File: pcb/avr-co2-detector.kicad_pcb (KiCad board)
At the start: 2 copper layers, 100 x 70 mm, 70 parts, among them J1 USB TYPE-C, J2 Backlight, J3 Backlight, J4 LCD0802, J5 AVR-ISP-10, J6 BH1.27-6-2, SW1 "Reset", SW2 "Reset", U1 ATtiny2313A-SU, U2 FT232RL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

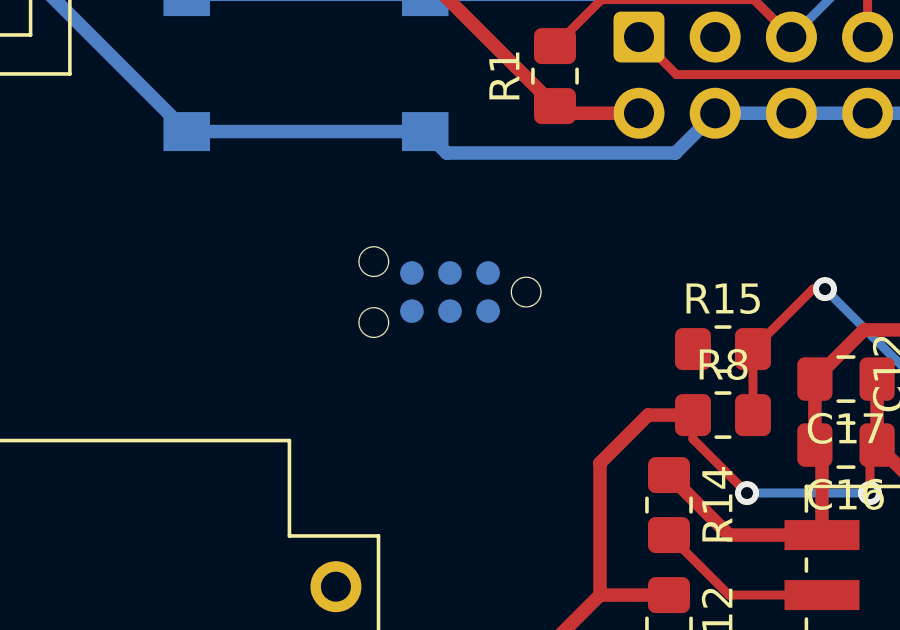
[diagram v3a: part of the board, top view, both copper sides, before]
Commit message: Corrected pull-up voltage on resistor R9, corrected footprint for connector J6
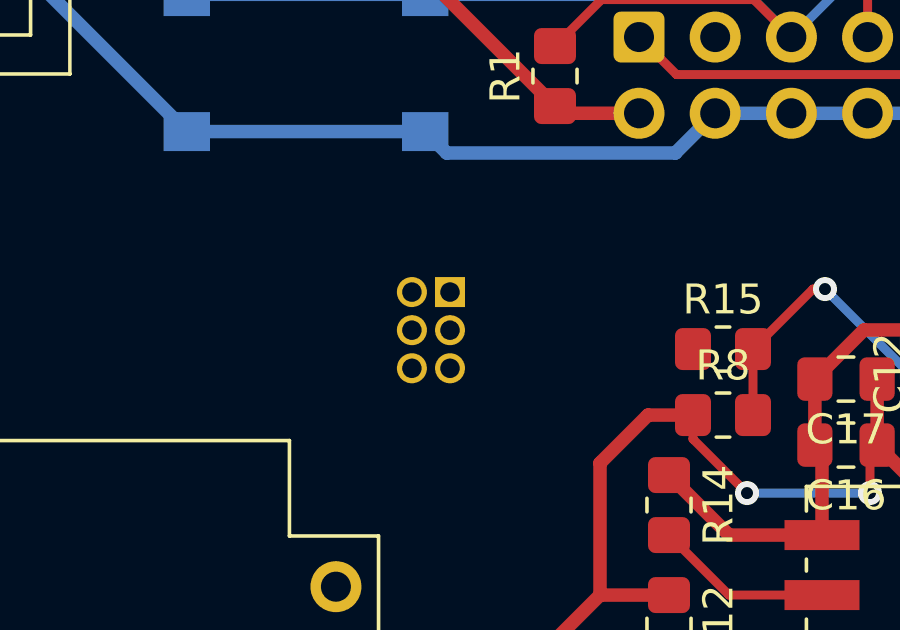
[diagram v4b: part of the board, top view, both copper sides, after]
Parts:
- J6: footprint Connector:Tag-Connect_TC2030-IDC-NL_2x03_P1.27mm_Vertical -> Connector_PinHeader_1.27mm:PinHeader_2x03_P1.27mm_Vertical
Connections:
- R9 pad 1: +5V -> +3.3V
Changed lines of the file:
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@@
     (fp_line (start -1 -0.625) (end 1 -0.625) (layer "F.Fab") (width 0.1))
     (pad "1" smd roundrect (at -1 0 90) (size 1.2 1.4) (layers "F.Cu" "F.Paste" "F.Mask") (roundrect_rratio 0.208333)
-      (net 5 "+5V") (pintype "passive"))
+      (net 9 "+3.3V") (pintype "passive"))
     (pad "2" smd roundrect (at 1 0 90) (size 1.2 1.4) (layers "F.Cu" "F.Paste" "F.Mask") (roundrect_rratio 0.208333)
       (net 8 "Net-(C14-Pad2)") (pintype "passive"))
@@
     )
   )
-  (footprint "Connector:Tag-Connect_TC2030-IDC-NL_2x03_P1.27mm_Vertical" (layer "B.Cu")
+  (footprint "Connector_PinHeader_1.27mm:PinHeader_2x03_P1.27mm_Vertical" (layer "B.Cu")
     (at 124.2 105.1 180)
-    (descr "Tag-Connect programming header; http://www.tag-connect.com/Materials/TC2030-IDC-NL.pdf")
-    (tags "tag connect programming header pogo pins")
-    (property "Sheetfile" "avr-co2-detector.kicad_sch")
-    (property "Sheetname" "")
-    (attr exclude_from_pos_files)
-    (fp_text reference "J6" (at 0 -2.7) (layer "B.SilkS")
-      (effects (font (size 1 1) (thickness 0.15)) (justify mirror))
-    )
-    (fp_text value "BH1.27-6-2" (at 0 2.3) (layer "B.Fab")
-      (effects (font (size 1 1) (thickness 0.15)) (justify mirror))
-    )
-    (fp_text user "KEEPOUT" (at 0 0) (layer "Cmts.User")
-      (effects (font (size 0.4 0.4) (thickness 0.07)))
-    )
-    (fp_text user "${REFERENCE}" (at 0 0) (layer "B.Fab")
-      (effects (font (size 1 1) (thickness 0.15)) (justify mirror))
-    )
-    (fp_line (start -1.905 -1.27) (end -1.905 -0.635) (layer "B.SilkS") (width 0.12))
-    (fp_line (start -1.27 -1.27) (end -1.905 -1.27) (layer "B.SilkS") (width 0.12))
-    (fp_line (start -3.5 2) (end 3.5 2) (layer "B.CrtYd") (width 0.05))
-    (fp_line (start 3.5 -2) (end -3.5 -2) (layer "B.CrtYd") (width 0.05))
-    (fp_line (start -3.5 -2) (end -3.5 2) (layer "B.CrtYd") (width 0.05))
-    (fp_line (start 3.5 2) (end 3.5 -2) (layer "B.CrtYd") (width 0.05))
-    (pad "" np_thru_hole circle (at 2.54 1.016 180) (size 0.9906 0.9906) (drill 0.9906) (layers *.Cu *.Mask))
-    (pad "" np_thru_hole circle (at 2.54 -1.016 180) (size 0.9906 0.9906) (drill 0.9906) (layers *.Cu *.Mask))
-    (pad "" np_thru_hole circle (at -2.54 0 180) (size 0.9906 0.9906) (drill 0.9906) (layers *.Cu *.Mask))
-    (pad "1" connect circle (at -1.27 -0.635 180) (size 0.7874 0.7874) (layers "B.Cu" "B.Mask")
+    (descr "Through hole straight pin header, 2x03, 1.27mm pitch, double rows")
+    (tags "Through hole pin header THT 2x03 1.27mm double row")
+    (property "Sheetfile" "avr-co2-detector.kicad_sch")
+    (property "Sheetname" "")
+    (attr through_hole)
+    (fp_text reference "J6" (at 0.635 1.695) (layer "B.SilkS")
+      (effects (font (size 1 1) (thickness 0.15)) (justify mirror))
+    )
+    (fp_text value "BH1.27-6-2" (at 0.635 -4.235) (layer "B.Fab")
+      (effects (font (size 1 1) (thickness 0.15)) (justify mirror))
+    )
+    (fp_text user "${REFERENCE}" (at 0.635 -1.27 90) (layer "B.Fab")
+      (effects (font (size 1 1) (thickness 0.15)) (justify mirror))
+    )
+    (fp_line (start 0.76 0.563471) (end 0.76 0.695) (layer "B.SilkS") (width 0.12))
+    (fp_line (start 0.563471 -0.76) (end 0.706529 -0.76) (layer "B.SilkS") (width 0.12))
+    (fp_line (start 1.57753 0.695) (end 2.4 0.695) (layer "B.SilkS") (width 0.12))
+    (fp_line (start 0.30753 -3.235) (end 0.96247 -3.235) (layer "B.SilkS") (width 0.12))
+    (fp_line (start -1.13 0.76) (end 0 0.76) (layer "B.SilkS") (width 0.12))
+    (fp_line (start -1.13 -0.76) (end -0.563471 -0.76) (layer "B.SilkS") (width 0.12))
+    (fp_line (start -1.13 0) (end -1.13 0.76) (layer "B.SilkS") (width 0.12))
+    (fp_line (start 1.57753 -3.235) (end 2.4 -3.235) (layer "B.SilkS") (width 0.12))
+    (fp_line (start -1.13 -3.235) (end -0.30753 -3.235) (layer "B.SilkS") (width 0.12))
+    (fp_line (start 2.4 0.695) (end 2.4 -3.235) (layer "B.SilkS") (width 0.12))
+    (fp_line (start 0.76 0.695) (end 0.96247 0.695) (layer "B.SilkS") (width 0.12))
+    (fp_line (start -1.13 -0.76) (end -1.13 -3.235) (layer "B.SilkS") (width 0.12))
+    (fp_line (start 0.76 -0.706529) (end 0.76 -0.563471) (layer "B.SilkS") (width 0.12))
+    (fp_line (start -1.6 -3.7) (end 2.85 -3.7) (layer "B.CrtYd") (width 0.05))
+    (fp_line (start -1.6 1.15) (end -1.6 -3.7) (layer "B.CrtYd") (width 0.05))
+    (fp_line (start 2.85 1.15) (end -1.6 1.15) (layer "B.CrtYd") (width 0.05))
+    (fp_line (start 2.85 -3.7) (end 2.85 1.15) (layer "B.CrtYd") (width 0.05))
+    (fp_line (start -1.07 -3.175) (end -1.07 -0.2175) (layer "B.Fab") (width 0.1))
+    (fp_line (start -1.07 -0.2175) (end -0.2175 0.635) (layer "B.Fab") (width 0.1))
+    (fp_line (start 2.34 -3.175) (end -1.07 -3.175) (layer "B.Fab") (width 0.1))
+    (fp_line (start -0.2175 0.635) (end 2.34 0.635) (layer "B.Fab") (width 0.1))
+    (fp_line (start 2.34 0.635) (end 2.34 -3.175) (layer "B.Fab") (width 0.1))
+    (pad "1" thru_hole rect (at 0 0 180) (size 1 1) (drill 0.65) (layers *.Cu *.Mask)
       (net 31 "/ESP_EN") (pinfunction "Pin_1") (pintype "passive"))
-    (pad "2" connect circle (at -1.27 0.635 180) (size 0.7874 0.7874) (layers "B.Cu" "B.Mask")
+    (pad "2" thru_hole oval (at 1.27 0 180) (size 1 1) (drill 0.65) (layers *.Cu *.Mask)
       (net 32 "/VDD") (pinfunction "Pin_2") (pintype "passive"))
-    (pad "3" connect circle (at 0 -0.635 180) (size 0.7874 0.7874) (layers "B.Cu" "B.Mask")
+    (pad "3" thru_hole oval (at 0 -1.27 180) (size 1 1) (drill 0.65) (layers *.Cu *.Mask)
       (net 33 "/ESP_TXD") (pinfunction "Pin_3") (pintype "passive"))
-    (pad "4" connect circle (at 0 0.635 180) (size 0.7874 0.7874) (layers "B.Cu" "B.Mask")
+    (pad "4" thru_hole oval (at 1.27 -1.27 180) (size 1 1) (drill 0.65) (layers *.Cu *.Mask)
       (net 1 "GND") (pinfunction "Pin_4") (pintype "passive"))
-    (pad "5" connect circle (at 1.27 -0.635 180) (size 0.7874 0.7874) (layers "B.Cu" "B.Mask")
+    (pad "5" thru_hole oval (at 0 -2.54 180) (size 1 1) (drill 0.65) (layers *.Cu *.Mask)
       (net 34 "/ESP_RXD") (pinfunction "Pin_5") (pintype "passive"))
-    (pad "6" connect circle (at 1.27 0.635 180) (size 0.7874 0.7874) (layers "B.Cu" "B.Mask")
+    (pad "6" thru_hole oval (at 1.27 -2.54 180) (size 1 1) (drill 0.65) (layers *.Cu *.Mask)
       (net 35 "/ESP_IO0") (pinfunction "Pin_6") (pintype "passive"))
-    (zone (net 0) (net_name "") (layer "B.Cu") (hatch full 0.508)
-      (connect_pads (clearance 0))
-      (min_thickness 0.254)
-      (keepout (tracks allowed) (vias not_allowed) (pads allowed) (copperpour not_allowed) (footprints not_allowed))
-      (fill (thermal_gap 0.508) (thermal_bridge_width 0.508))
-      (polygon
-        (pts
-          (xy 122.93 104.465)
-          (xy 125.47 104.465)
-          (xy 125.47 105.735)
-          (xy 122.93 105.735)
-        )
-      )
-    )
-  )
+    (model "${KICAD6_3DMODEL_DIR}/Connector_PinHeader_1.27mm.3dshapes/PinHeader_2x03_P1.27mm_Vertical.wrl"
+      (offset (xyz 0 0 0))
+      (scale (xyz 1 1 1))
+      (rotate (xyz 0 0 0))
+    )
+  )

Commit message: Finished routing
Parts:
- moved U7 52.0 mm to (109.4, 119.2)
- moved C20 52.0 mm to (113.6, 119.2)
- moved C23 52.0 mm to (109.5, 115.6)
- moved J6 2.92 mm to (126.0, 107.4)
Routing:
- net /AVR_DEBUG_RXD: track 0.00 -> 138.7 mm, vias 0 -> 4
- net /ESP_TXD: track 0.00 -> 108.5 mm, vias 0 -> 3
- net /ESP_DEBUG_RXD: track 0.00 -> 102.5 mm, vias 0 -> 3
- net +3.3V: track 146.0 -> 220.4 mm, vias 2 -> 4
- net /AVR_RXD: track 0.00 -> 71.8 mm, vias 0 -> 3
- net Net-(JP1-Pad2): track 0.00 -> 61.3 mm, vias 0 -> 1
- net +5V: track 219.9 -> 275.3 mm, vias 0 -> 3
- net Net-(R16-Pad2): track 4.34 -> 58.0 mm, vias 0 -> 3
- net Net-(U1-Pad2): track 0.00 -> 53.3 mm, vias 0 -> 1
- net GND: track 457.0 -> 505.0 mm, vias 2 -> 5
- net Net-(U1-Pad3): track 0.00 -> 47.7 mm, vias 0 -> 1
- net Net-(JP1-Pad1): track 0.00 -> 40.7 mm, vias 0 -> 2
- net /ESP_DEBUG_TXD: track 0.00 -> 39.5 mm, vias 0 -> 1
- net /AVR_TXD: track 0.00 -> 37.9 mm, vias 0 -> 3
- net /RS: track 0.00 -> 34.3 mm, vias 0 -> 1
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
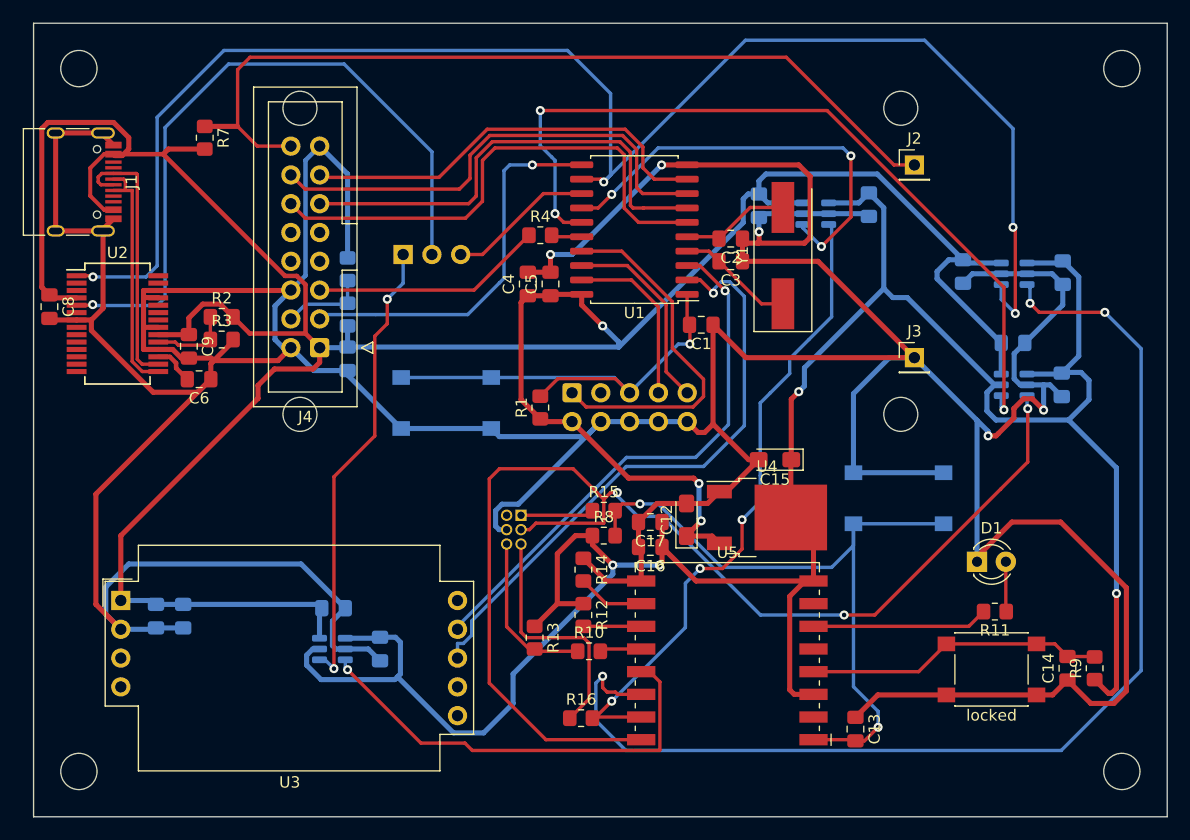
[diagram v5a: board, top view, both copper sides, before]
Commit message: Added GND polygons
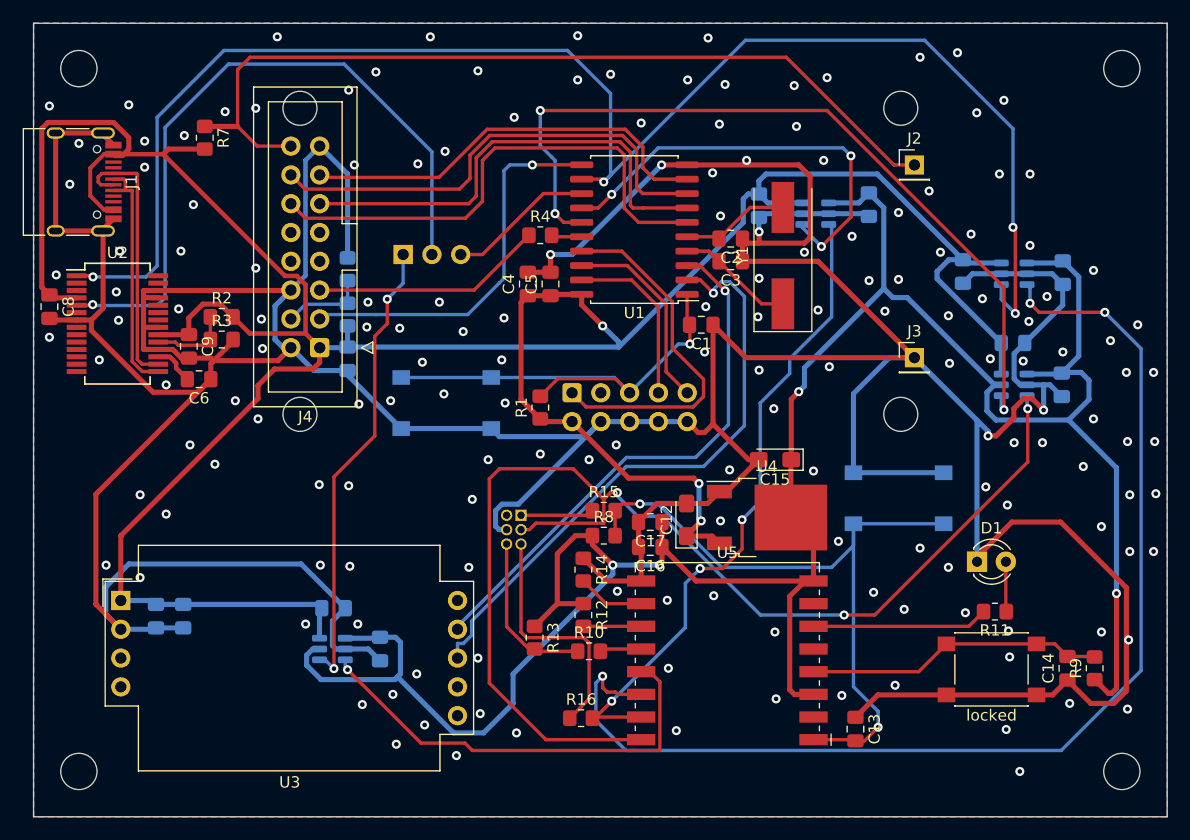
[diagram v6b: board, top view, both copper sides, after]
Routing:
- net GND: vias 5 -> 168
- added copper zone on B.Cu, net GND
- added copper zone on F.Cu, net GND

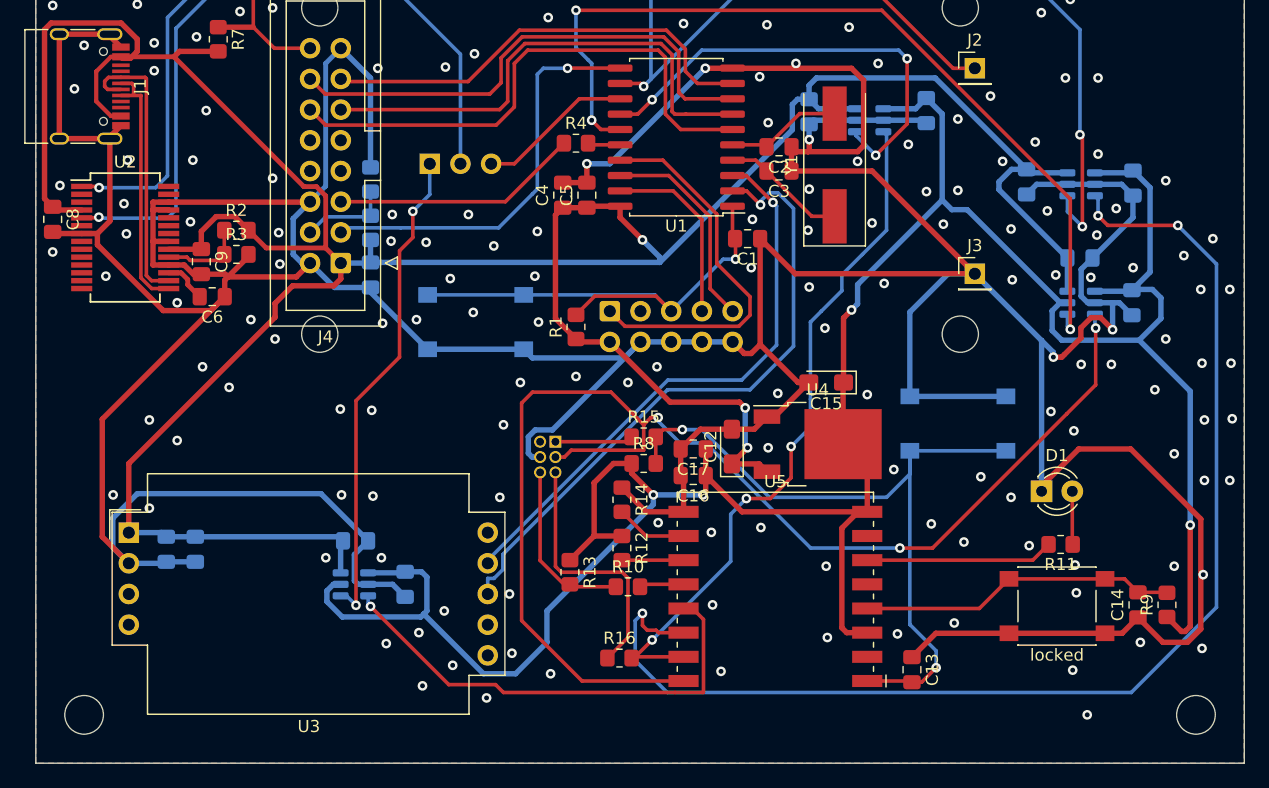
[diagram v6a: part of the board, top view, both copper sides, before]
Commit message: Fixed DRC errors and warnings
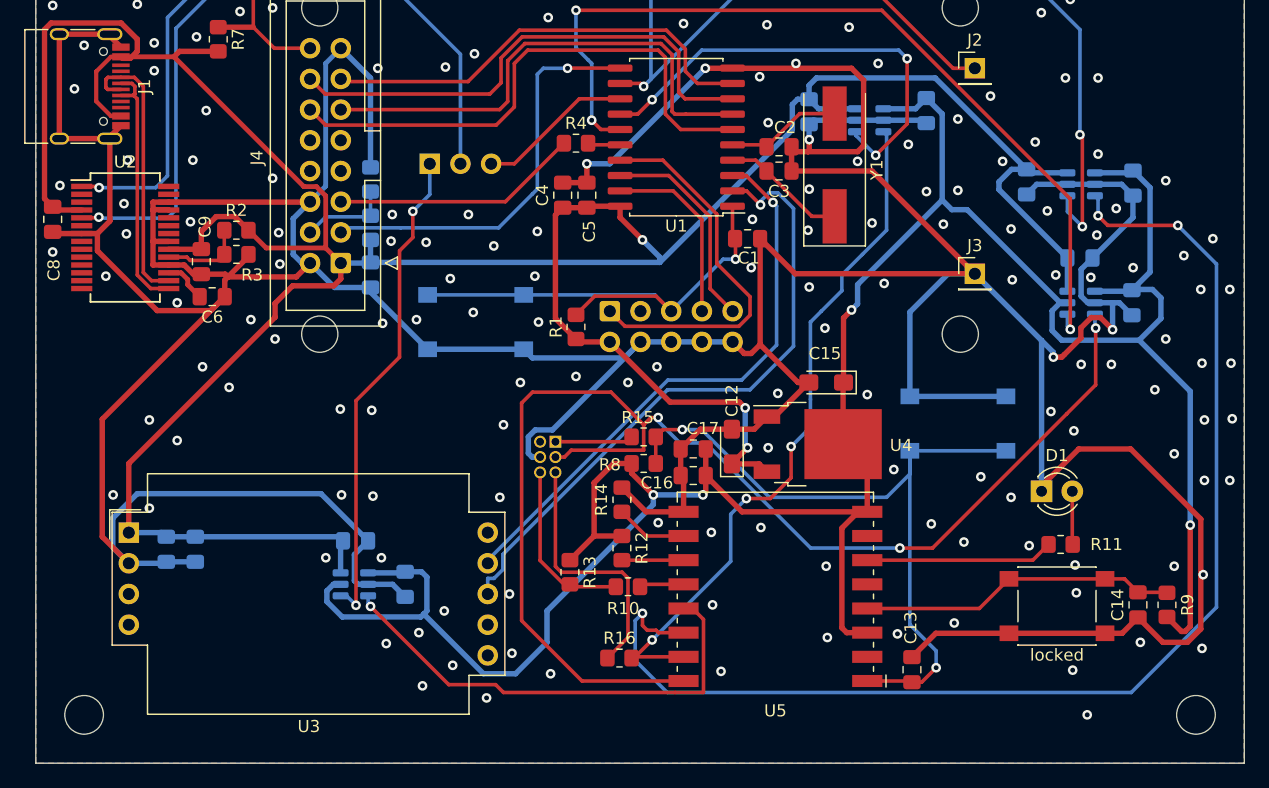
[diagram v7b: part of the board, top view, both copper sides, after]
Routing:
- net Net-(J1-PadA6): track 22.4 -> 21.2 mm
- net Net-(J1-PadA7): track 23.8 -> 23.3 mm
